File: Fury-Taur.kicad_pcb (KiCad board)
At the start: 2 copper layers, 75.1 x 26.5 mm, 31 parts, among them J1 Pickup, J2 Output, Q1 Bias 20K, Q1 J201, Q1 Test TestPoint_THTPad_1.0x1.0mm_Dr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, Q2 Bias 20K, Q2 J201, Q2 Test TestPoint_THTPad_1.0x1.0mm_Dr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, SW1 ALPHA_PUSH_PULL, SW2 SW_SPDT

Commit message: Change footprint of terminal blocks
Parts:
- J1: footprint TerminalBlock_4Ucon:TerminalBlock_4Ucon_1x05_P3.50mm_Horizontal -> TerminalBlock_Phoenix:TerminalBlock_Phoenix_PT-1,5-5-3.5-H_1x05_P3.50mm_Horizontal
- J2: footprint TerminalBlock_4Ucon:TerminalBlock_4Ucon_1x03_P3.50mm_Horizontal -> TerminalBlock_Phoenix:TerminalBlock_Phoenix_PT-1,5-3-3.5-H_1x03_P3.50mm_Horizontal
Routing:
- net Net-(R5-Pad2): track 52.2 -> 51.4 mm

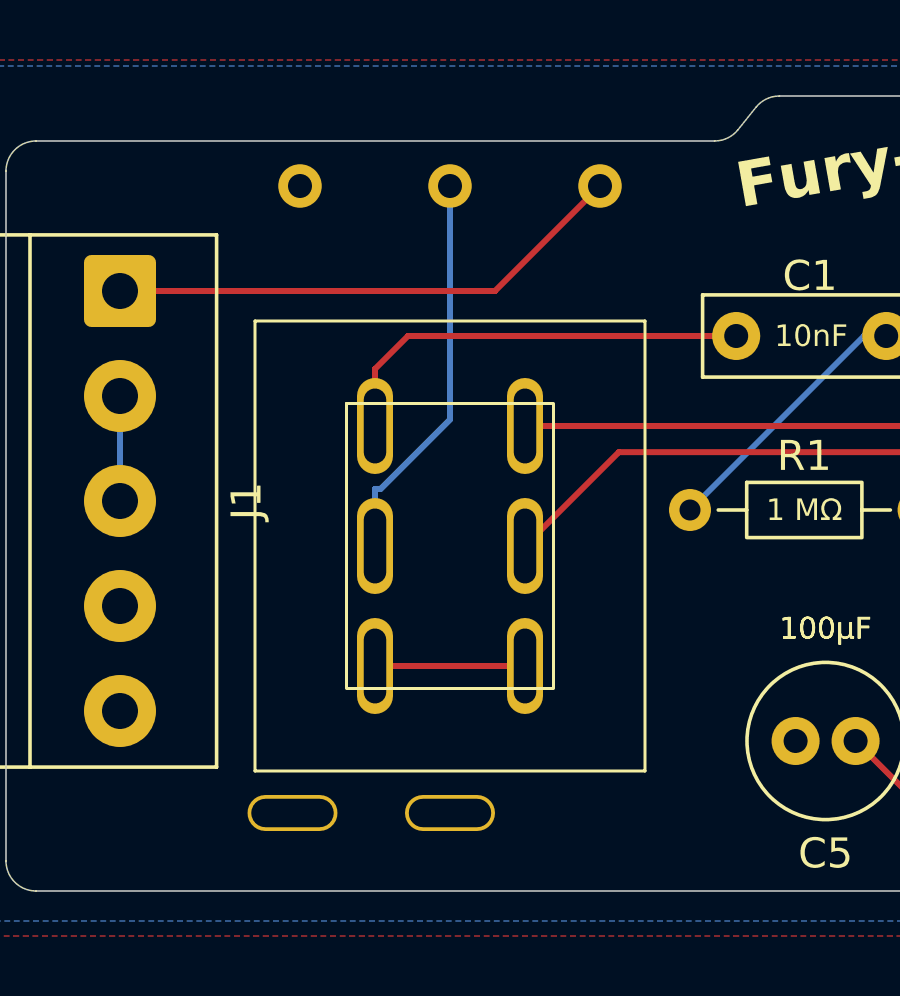
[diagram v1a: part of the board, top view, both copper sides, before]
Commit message: Better 3D model of Push/Pull Switch. Updated footprint of Push/Pull Switch
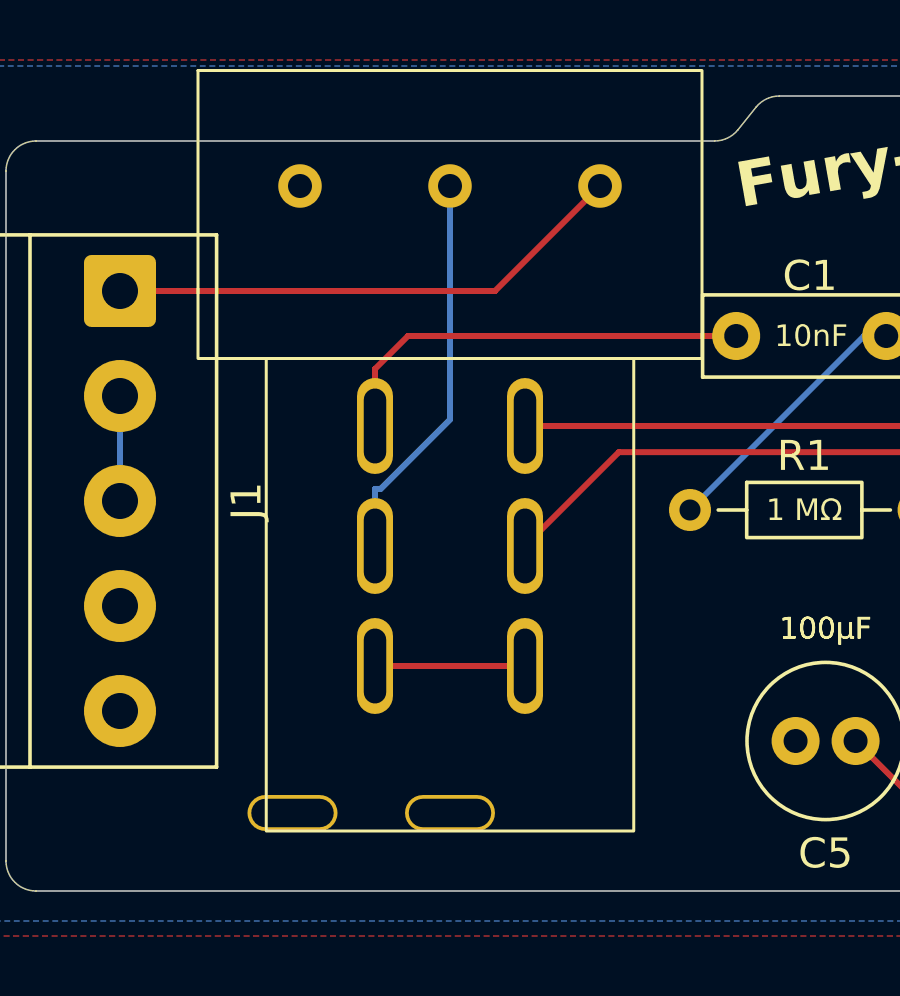
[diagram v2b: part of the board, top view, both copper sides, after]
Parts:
- removed PushPushGround: , Custom:PushPushGround
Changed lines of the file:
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@@
 		)
 	)
-	(footprint "Custom:PushPushGround"
-		(layer "F.Cu")
-		(at 87.75 86.4)
-		(property "Reference" "PushPushGround"
-			(at 0 0 0)
-			(layer "F.SilkS")
-			(hide yes)
-			(effects
-				(font
-					(size 1.27 1.27)
-				)
-			)
-		)
-		(property "Value" ""
-			(at 0 0 0)
-			(layer "F.SilkS")
-			(effects
-				(font
-					(size 1.27 1.27)
-				)
-			)
-		)
-		(property "Datasheet" ""
-			(at 0 0 0)
-			(layer "F.Fab")
-			(hide yes)
-			(effects
-				(font
-					(size 1.27 1.27)
-				)
-			)
-		)
-		(property "Description" ""
-			(at 0 0 0)
-			(layer "F.Fab")
-			(hide yes)
-			(effects
-				(font
-					(size 1.27 1.27)
-				)
-			)
-		)
-		(duplicate_pad_numbers_are_jumpers no)
-		(pad "10" thru_hole oval
-			(at 0 0)
-			(size 3 1.2)
-			(drill oval 2.75 0.95)
-			(layers "*.Cu" "*.Mask")
-			(remove_unused_layers yes)
-			(keep_end_layers yes)
-			(zone_layer_connections)
-			(net "GND")
-			(teardrops
-				(best_length_ratio 0.5)
-				(max_length 1)
-				(best_width_ratio 1)
-				(max_width 2)
-				(curved_edges no)
-				(filter_ratio 0.9)
-				(enabled yes)
-				(allow_two_segments yes)
-				(prefer_zone_connections yes)
-			)
-		)
-		(embedded_fonts no)
-	)
 	(footprint "Capacitor_THT:C_Disc_D4.7mm_W2.5mm_P5.00mm"
 		(layer "F.Cu")
@@
 		(duplicate_pad_numbers_are_jumpers no)
 		(fp_rect
-			(start -3.45 -4.75)
-			(end 3.45 4.75)
+			(start -8.4 -15.85)
+			(end 8.4 -6.25)
+			(radius 0.4)
+			(stroke
+				(width 0.1)
+				(type default)
+			)
+			(fill no)
+			(layer "F.SilkS")
+		)
+		(fp_rect
+			(start -6.125 -6.25)
+			(end 6.125 9.5)
 			(stroke
 				(width 0.1)
@@
 			)
 		)
+		(pad "11" thru_hole oval
+			(at -5.25 8.9)
+			(size 3 1.2)
+			(drill oval 2.75 0.95)
+			(layers "*.Cu" "*.Mask")
+			(remove_unused_layers yes)
+			(keep_end_layers yes)
+			(zone_layer_connections)
+			(net "GND")
+			(teardrops
+				(best_length_ratio 0.5)
+				(max_length 1)
+				(best_width_ratio 1)
+				(max_width 2)
+				(curved_edges no)
+				(filter_ratio 0.9)
+				(enabled yes)
+				(allow_two_segments yes)
+				(prefer_zone_connections yes)
+			)
+		)
 		(embedded_fonts no)
-		(model "${KICAD10_3DMODEL_DIR}/PushPullSwitch.3dshapes/User Library-Switch_Pot_Small_Shaft.STEP"
+		(model "${KICAD10_3DMODEL_DIR}/PushPullSwitch.3dshapes/User Library-Switch_Pot_Small_Shaft.step"
 			(offset
 				(xyz 9 8 -7)
 			)
 			(scale
-				(xyz 1 0.9 1)
+				(xyz 1 1.05 1.04)
 			)
 			(rotate
@@
 		)
 	)
-	(gr_rect
-		(start 86.5 70)
-		(end 99.5 85)
-		(stroke
-			(width 0.1)
-			(type default)
-		)
-		(fill no)
-		(layer "F.SilkS")
-	)
 	(gr_arc

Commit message: Made single library entry for Push Pull Switch. Updated schematic and PCB with the entry
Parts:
- removed RV1J: TO_POT_LUGS, Custom:Pot_Lug_Jumper_Pads_Above_SW
- removed SW1: ALPHA_PUSH_PULL, Custom:Alpha_PushPull_DirectSwitch_TightSlots
- added REF**: PushPull_Pot_DPDT, Custom:PushPull_Pot_DPDT, F.Cu at (93.0, 77.5)

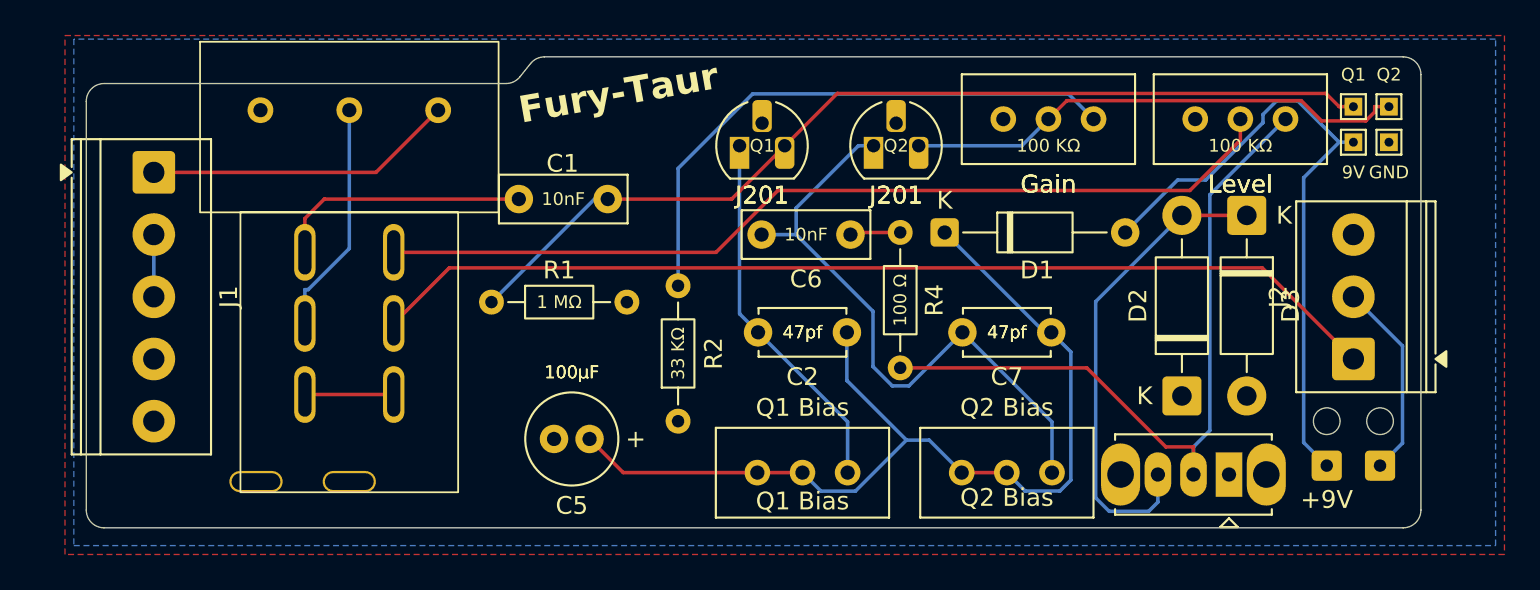
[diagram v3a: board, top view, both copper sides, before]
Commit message: Was missing C3, other board versions will not work
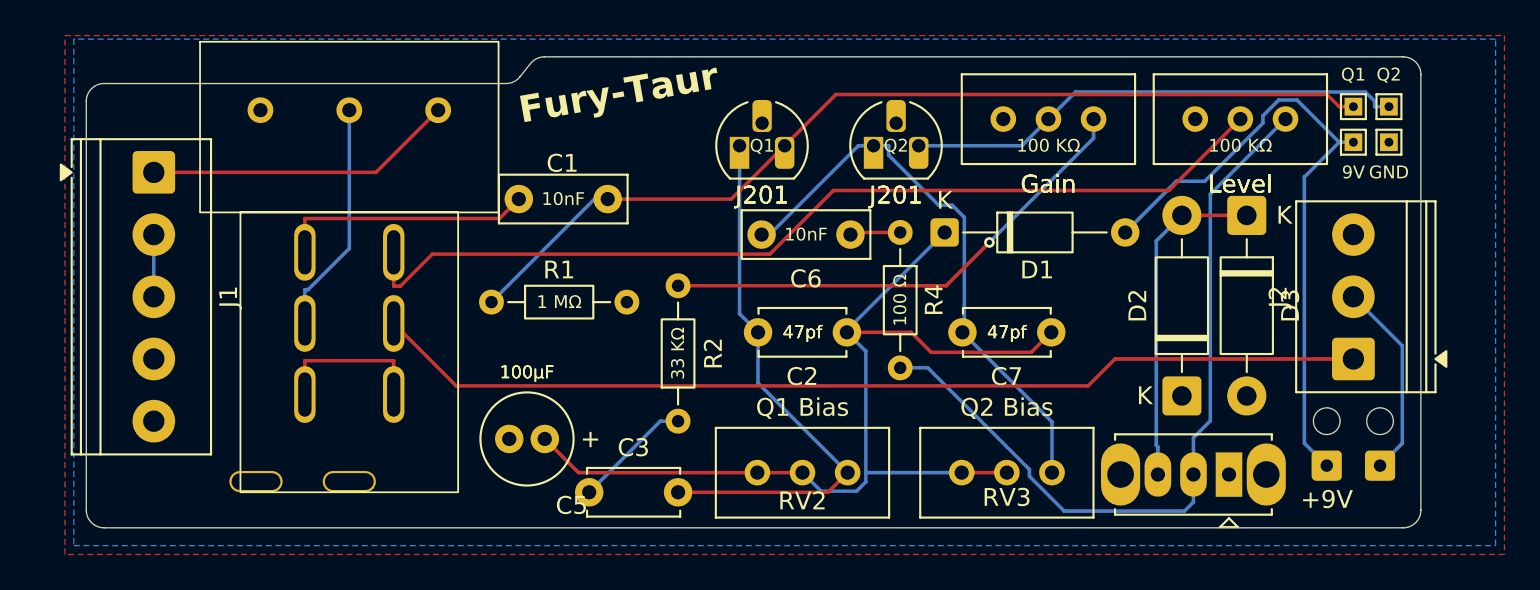
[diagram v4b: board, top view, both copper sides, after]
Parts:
- added C3: C_Disc_D5.0mm_W2.5mm_P5.00mm, Capacitor_THT:C_Disc_D5.0mm_W2.5mm_P5.00mm, F.Cu at (106.5, 87.0)
- RV2: renamed from Q1 Bias
- RV3: renamed from Q2 Bias
- moved C5 2.52 mm to (104.0, 84.0)
- renumbered REF** to RV1
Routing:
- net Net-(Q1-D): track 20.9 -> 30.9 mm
- net Net-(D2-A): track 27.1 -> 18.9 mm
- net Net-(C3-Pad1): track 0.00 -> 6.66 mm
- net Net-(R2-Pad2): track 32.3 -> 27.9 mm, vias 0 -> 1
- net COMMON: track 5.00 -> 8.80 mm
- net Net-(Q2-D): track 35.2 -> 32.0 mm
- net Net-(R5-Pad2): track 51.4 -> 53.4 mm
- net Net-(SW2-B): track 42.0 -> 44.0 mm
- net Net-(D1-K): track 55.1 -> 56.6 mm
- net VOL_OUT_TO_JACK_TIP: track 57.4 -> 56.1 mm

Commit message: Updated various behind the scenes things, such as C5 polarazed symbol, J201 datasheet, add #PWR_FLAG to power
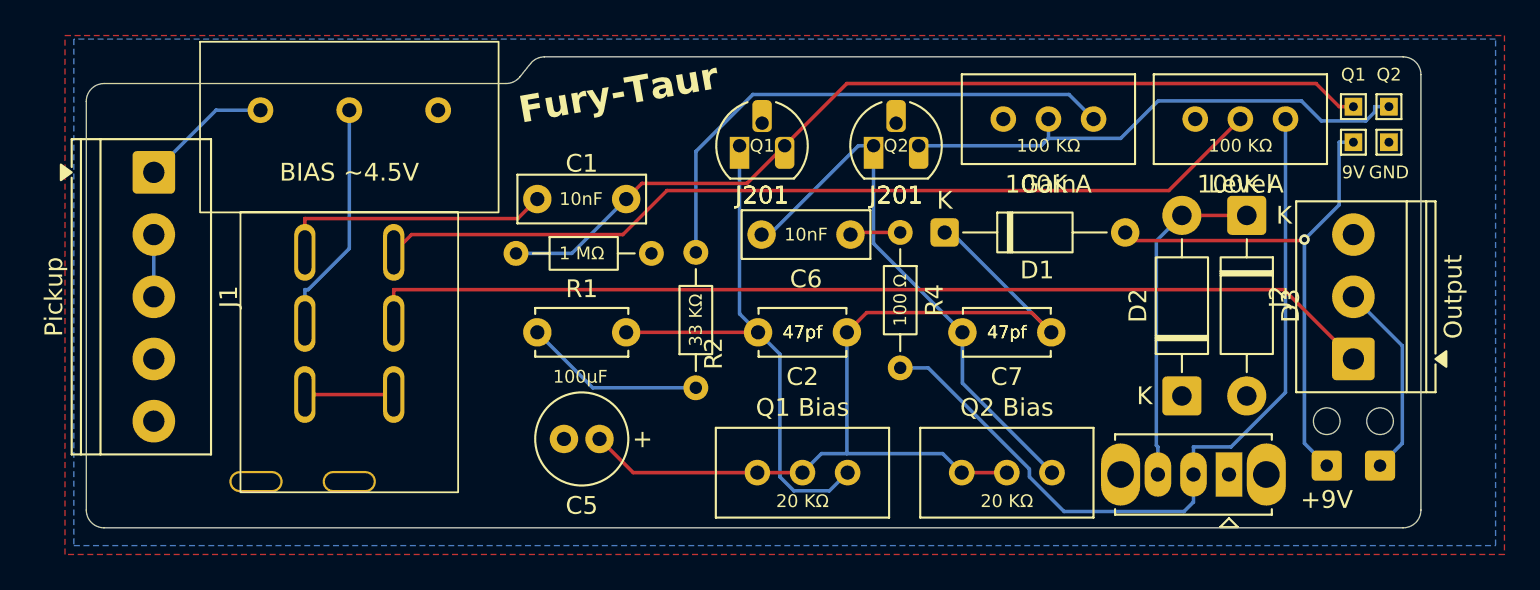
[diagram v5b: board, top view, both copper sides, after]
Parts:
- C3: value C_Disc_D5.0mm_W2.5mm_P5.00mm -> 4.7nf
- C5: value 100μF -> 100uf
- R3: value Gain -> 100K A
- R5: value Level -> 100K A
- RV1: value PushPull_Pot_DPDT -> ~
- moved C3 9.46 mm to (103.6, 78.0)
- moved C5 3.08 mm to (107.1, 84.0)
- moved R1 3.07 mm to (102.4, 73.6)
- moved R2 2.13 mm to (112.5, 81.1)
- moved C1 1.04 mm to (108.6, 70.5)
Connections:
- net COMMON renamed Net-(RV1B-A2)
- net VOL_OUT_TO_JACK_TIP renamed Net-(J2-Pin_1)
- net VOL_OUT_TO_SWITCH renamed Net-(RV1A-Wiper)
- J1 pad 5: PU_NORTH_START -> Net-(J1-Pin_5)
- RV1 pad 1: GND -> Net-(J1-Pin_5)
- RV1 pad 10: (no net) -> GND
- RV1 pad 3: PU_NORTH_START -> GND
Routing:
- net PU_NORTH_START: track 17.4 -> 0.00 mm
- net Net-(J1-Pin_5): track 0.00 -> 7.45 mm
- net +9V: track 36.7 -> 30.0 mm, vias 0 -> 1
- net Net-(D1-K): track 56.6 -> 51.8 mm
- net Net-(RV1B-A2): track 8.80 -> 5.00 mm
- net Net-(C3-Pad1): track 6.66 -> 10.2 mm
- net Net-(RV1B-B1): track 53.4 -> 50.7 mm
- net Net-(R2-Pad2): track 27.9 -> 30.0 mm, vias 1 -> 0
- net Net-(Q1-G): track 53.6 -> 51.6 mm
- net Net-(Q2-D): track 32.0 -> 30.5 mm
- net Net-(J2-Pin_1): track 56.1 -> 57.5 mm
- net Net-(Q2-G): track 28.2 -> 29.6 mm
- net Net-(SW2-B): track 44.0 -> 45.3 mm
- net Net-(RV1B-A1): track 14.4 -> 15.4 mm
- net Net-(Q1-D): track 30.9 -> 31.6 mm
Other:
- board text added: "20 KΩ"
- board text added: "BIAS ~4.5V"

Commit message: Updated various behind the scenes things, such as C5 polarazed symbol, J201 datasheet, add #PWR_FLAG to power
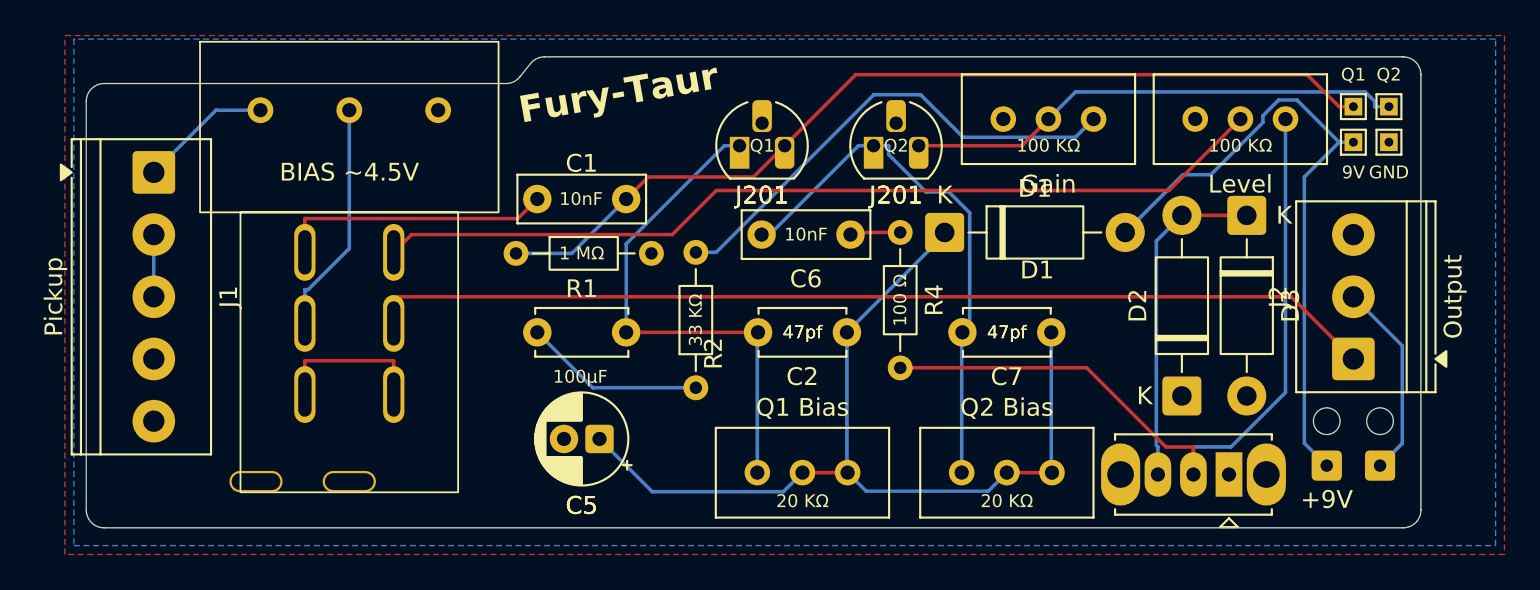
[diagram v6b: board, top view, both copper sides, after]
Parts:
- C5: footprint Capacitor_THT:C_Radial_D5.0mm_H11.0mm_P2.00mm -> Capacitor_THT:CP_Radial_D5.0mm_P2.00mm
- D1: footprint Diode_THT:D_DO-35_SOD27_P10.16mm_Horizontal -> Diode_THT:D_DO-41_SOD81_P10.16mm_Horizontal
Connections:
- RV2 pad 1: Net-(Q1-D) -> Net-(D1-K)
- RV2 pad 3: Net-(D1-K) -> Net-(Q1-D)
- RV3 pad 1: Net-(Q2-D) -> Net-(D1-K)
- RV3 pad 3: Net-(D1-K) -> Net-(Q2-D)
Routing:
- net +9V: track 30.0 -> 36.7 mm, vias 1 -> 0
- net Net-(RV1B-A2): track 5.00 -> 8.80 mm
- net Net-(Q1-D): track 31.6 -> 29.0 mm
- net Net-(R2-Pad2): track 30.0 -> 27.5 mm
- net Net-(SW2-B): track 45.3 -> 43.3 mm
- net Net-(Q2-G): track 29.6 -> 28.2 mm
- net Net-(J2-Pin_1): track 57.5 -> 56.9 mm
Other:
- board text removed: "+"

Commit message: Re-Annotated components
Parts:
- renumbered C5 to C4, C6 to C5, C7 to C6, R4 to R3, R3 to RV4, R5 to RV5, SW2 to SW1
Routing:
- net Net-(RV1B-A2): track 8.80 -> 5.00 mm
- net Net-(Q2-D): track 30.4 -> 29.4 mm
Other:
- board text removed: "C5"

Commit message: Re-Annotated components
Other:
- board text added: "C3"
- board text added: "C4"
- board text added: "C5"
- board text added: "R3"
- board text removed: "C7"
- board text removed: "R4"
